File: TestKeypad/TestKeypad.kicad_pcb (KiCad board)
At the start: 2 copper layers, 78.7 x 92.7 mm, 71 parts, among them J1 Mini-DIN-6, Q1 2N7000, SW1 SW_SPST, SW10 SW_SPST, SW11 SW_SPST, SW12 SW_SPST, SW13 SW_SPST, SW14 SW_SPST, SW15 SW_SPST, SW16 SW_SPST, SW2 SW_SPST, SW3 SW_SPST, SW4 SW_SPST, SW5 SW_SPST, SW6 SW_SPST, SW7 SW_SPST, SW8 SW_SPST, SW9 SW_SPST, U1 ATtiny24A-PU

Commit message: Finalise test keypad r01 and silkscreen
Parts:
- added REF**: OSHW Logo, Symbol:OSHW-Symbol_6.7x6mm_SilkScreen, F.Cu at (177.5, 69.8)
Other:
- board text added: "JLCJLCJLCJLC"
- board text added: "Order:"
- board text added: "PS2KB Testpad"
- board text added: "r01"

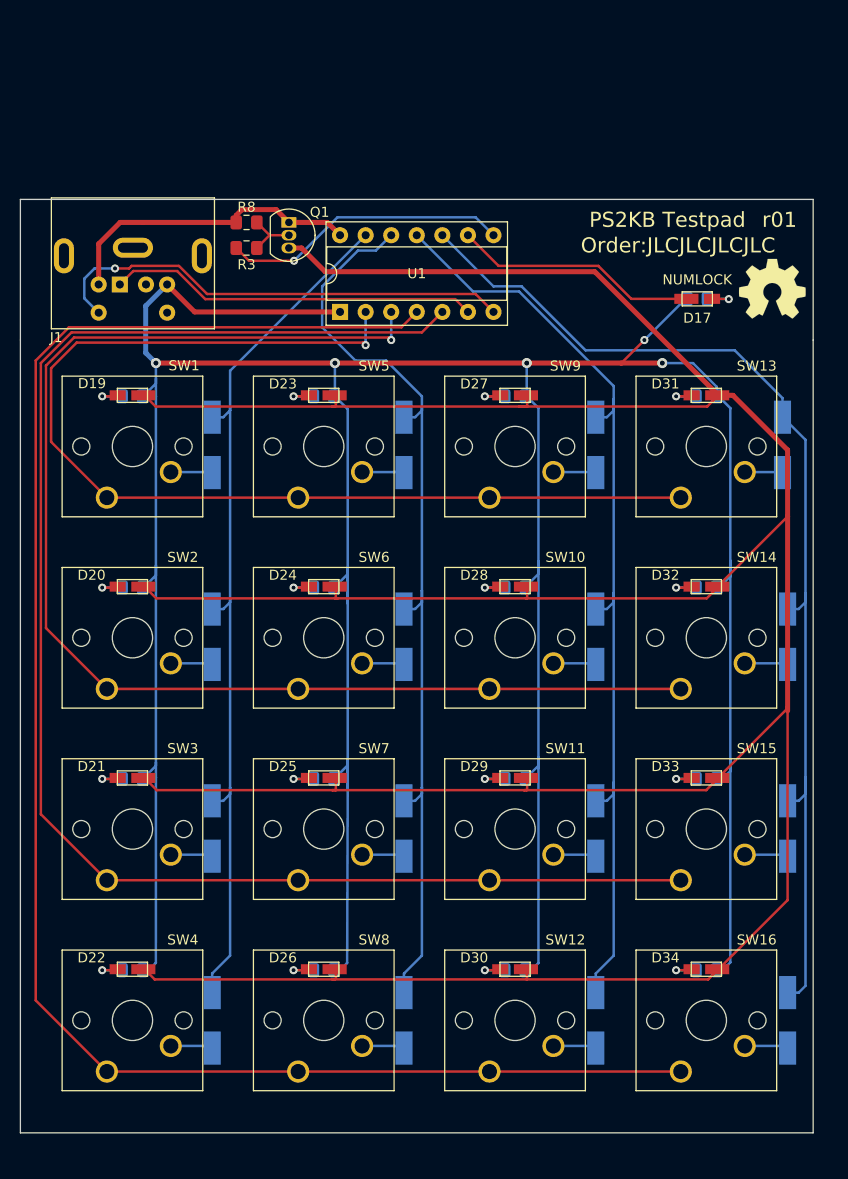
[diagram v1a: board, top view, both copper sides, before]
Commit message: Revise test keypad to r02
Updated components to match the actual board and revised PCB layout
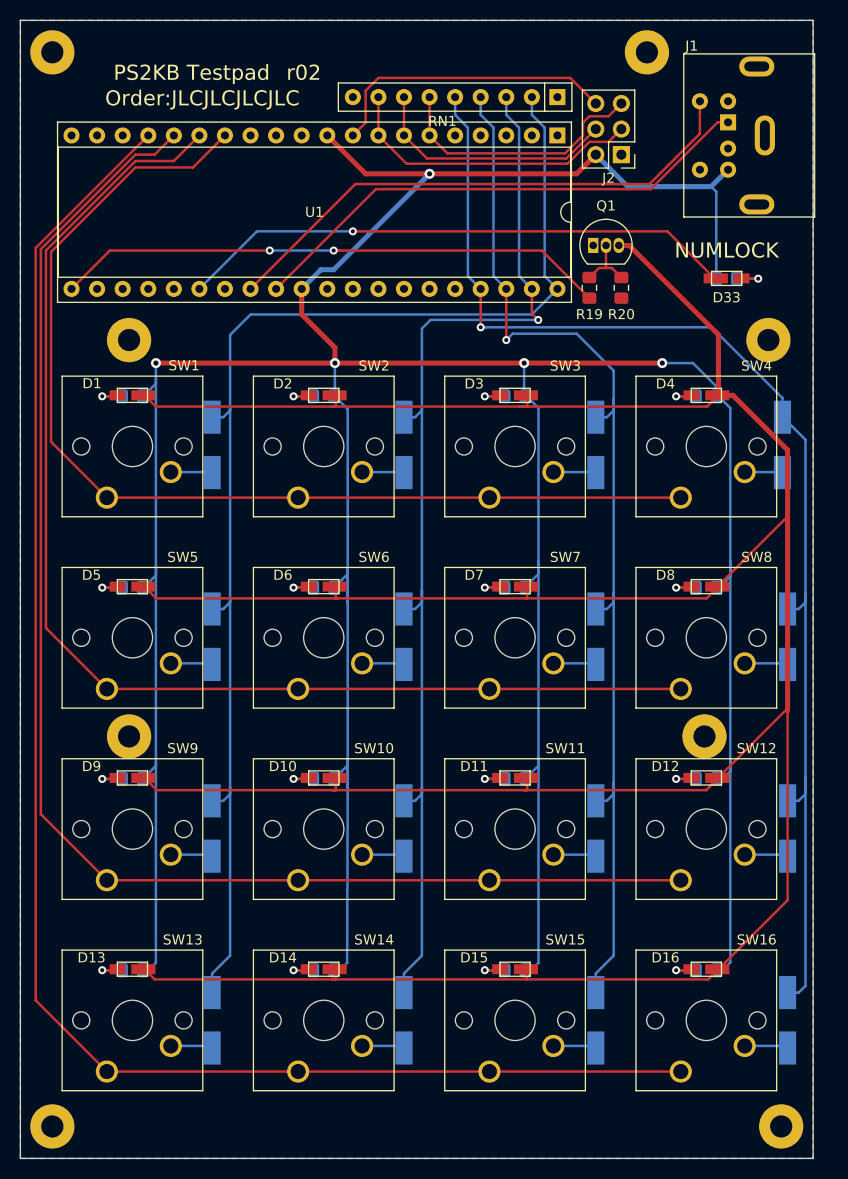
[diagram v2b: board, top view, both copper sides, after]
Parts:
- removed the REF** at (177.5, 69.8)
- added J2: ISP Header, Connector_PinHeader_2.54mm:PinHeader_2x03_P2.54mm_Vertical, F.Cu at (162.6, 56.5)
- added REF**: MountingHole_2.2mm_M2_Pad, MountingHole:MountingHole_2.2mm_M2_Pad, F.Cu at (113.7, 114.3)
- added REF**: MountingHole_2.2mm_M2_Pad, MountingHole:MountingHole_2.2mm_M2_Pad, F.Cu at (170.8, 114.3)
- added REF**: MountingHole_2.2mm_M2_Pad, MountingHole:MountingHole_2.2mm_M2_Pad, F.Cu at (106.0, 153.0)
- added REF**: MountingHole_2.2mm_M2_Pad, MountingHole:MountingHole_2.2mm_M2_Pad, F.Cu at (178.4, 153.0)
- added REF**: MountingHole_2.2mm_M2_Pad, MountingHole:MountingHole_2.2mm_M2_Pad, F.Cu at (177.2, 74.9)
- added REF**: MountingHole_2.2mm_M2_Pad, MountingHole:MountingHole_2.2mm_M2_Pad, F.Cu at (113.7, 74.9)
- added REF**: MountingHole_2.2mm_M2_Pad, MountingHole:MountingHole_2.2mm_M2_Pad, F.Cu at (165.1, 46.4)
- added REF**: MountingHole_2.2mm_M2_Pad, MountingHole:MountingHole_2.2mm_M2_Pad, F.Cu at (106.0, 46.4)
- added RN1: 100k, Resistor_THT:R_Array_SIP9, F.Cu at (156.2, 50.8)
- U1: value ATtiny24A-PU -> ATmega8535-16PU; footprint Package_DIP:DIP-14_W7.62mm_Socket -> Package_DIP:DIP-40_W15.24mm_Socket
- moved J1 62.5 mm to (175.3, 54.6), turned to 90 degrees
- moved R20 37.8 mm to (162.6, 69.7), turned to 270 degrees
- moved R19 34.3 mm to (159.4, 69.7), turned to 90 degrees
- moved Q1 30.3 mm to (159.8, 65.5), turned to 0 degrees
- moved U1 27.8 mm to (156.2, 54.6), turned to 270 degrees
- moved D33 3.56 mm to (173.0, 68.8)
- moved R17 3.56 mm to (173.0, 68.8)
- renumbered D19 to D1, D25 to D10, D29 to D11, D33 to D12, D22 to D13, D26 to D14, D30 to D15, D34 to D16, D1 to D17, D5 to D18, D9 to D19, D23 to D2, D13 to D20, D2 to D21, D6 to D22, D10 to D23, D14 to D24, D3 to D25, D7 to D26, D11 to D27, D15 to D28, D4 to D29, D27 to D3, D8 to D30, D12 to D31, D16 to D32, D17 to D33, D31 to D4, D20 to D5, D24 to D6, D28 to D7, D32 to D8, D21 to D9, R4 to R1, R11 to R10, R15 to R11, R19 to R12, R7 to R13, R12 to R14, R16 to R15, R20 to R16, R1 to R17, R3 to R19, R9 to R2, R8 to R20, R13 to R3, R17 to R4, R10 to R6, R14 to R7, R18 to R8, R6 to R9, SW7 to SW10, SW15 to SW12, SW4 to SW13, SW8 to SW14, SW12 to SW15, SW5 to SW2, SW9 to SW3, SW13 to SW4, SW2 to SW5, SW10 to SW7, SW14 to SW8, SW3 to SW9
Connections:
- D33 pad 1: Net-(D17-Pad1) -> Net-(D33-Pad1)
- J1 pad 3: Earth -> GND
- R19 pad 1: Net-(Q1-Pad2) -> /Counter2A-PWM
- R19 pad 2: /LED-PWM -> Net-(Q1-Pad2)
- U1 pad 1: 5v -> Earth
- U1 pad 10: D -> 5v
- U1 pad 11: C -> Earth
- U1 pad 12: B -> Net-(U1-Pad12)
- U1 pad 13: A -> Net-(U1-Pad13)
- U1 pad 14: Earth -> 1
- U1 pad 2: 1 -> Earth
- U1 pad 3: 2 -> Earth
- U1 pad 4: 4 -> Earth
- U1 pad 5: 3 -> Earth
- U1 pad 6: /Data -> Net-(J2-Pad5)
- U1 pad 7: /Clk -> Net-(J2-Pad4)
- U1 pad 8: /LED-PWM -> Net-(J2-Pad3)
- U1 pad 9: Net-(D17-Pad1) -> Net-(J2-Pad6)
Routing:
- net Net-(D33-Pad1): track 0.00 -> 55.5 mm, vias 0 -> 1
- net /Counter2A-PWM: track 0.00 -> 55.0 mm, vias 0 -> 2
- net 5v: track 368.6 -> 411.8 mm
- net A: track 89.1 -> 128.1 mm
- net Earth: track 30.9 -> 0.00 mm
- net Net-(J2-Pad3): track 0.00 -> 30.5 mm
- net Net-(J2-Pad6): track 0.00 -> 29.4 mm
- net Net-(D1-Pad1): track 375.0 -> 345.9 mm
- net /LED-PWM: track 28.8 -> 0.00 mm, vias 1 -> 0
- net Net-(J2-Pad5): track 0.00 -> 26.4 mm
- net Net-(J2-Pad4): track 0.00 -> 25.0 mm
- net Net-(D17-Pad1): track 24.2 -> 0.00 mm
- net B: track 94.1 -> 110.4 mm, vias 0 -> 1
- net D: track 108.5 -> 124.9 mm, vias 0 -> 1
- net /Data: track 36.8 -> 51.7 mm
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- added copper zone on B.Cu, net Earth
- added copper zone on F.Cu, net Earth
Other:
- board size 78.7 x 92.7 mm -> 78.7 x 113 mm
- board text added: "r02"
- board text removed: "r01"

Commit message: Revise test keypad to r03
Tweaked just before making a production run
Added screw holes
Added an ISP header
Added pulldown resistor array to switch input lines
Also remapped an incorrectly-placed "GND" label to the actual ground net (which slipped through into the production run)
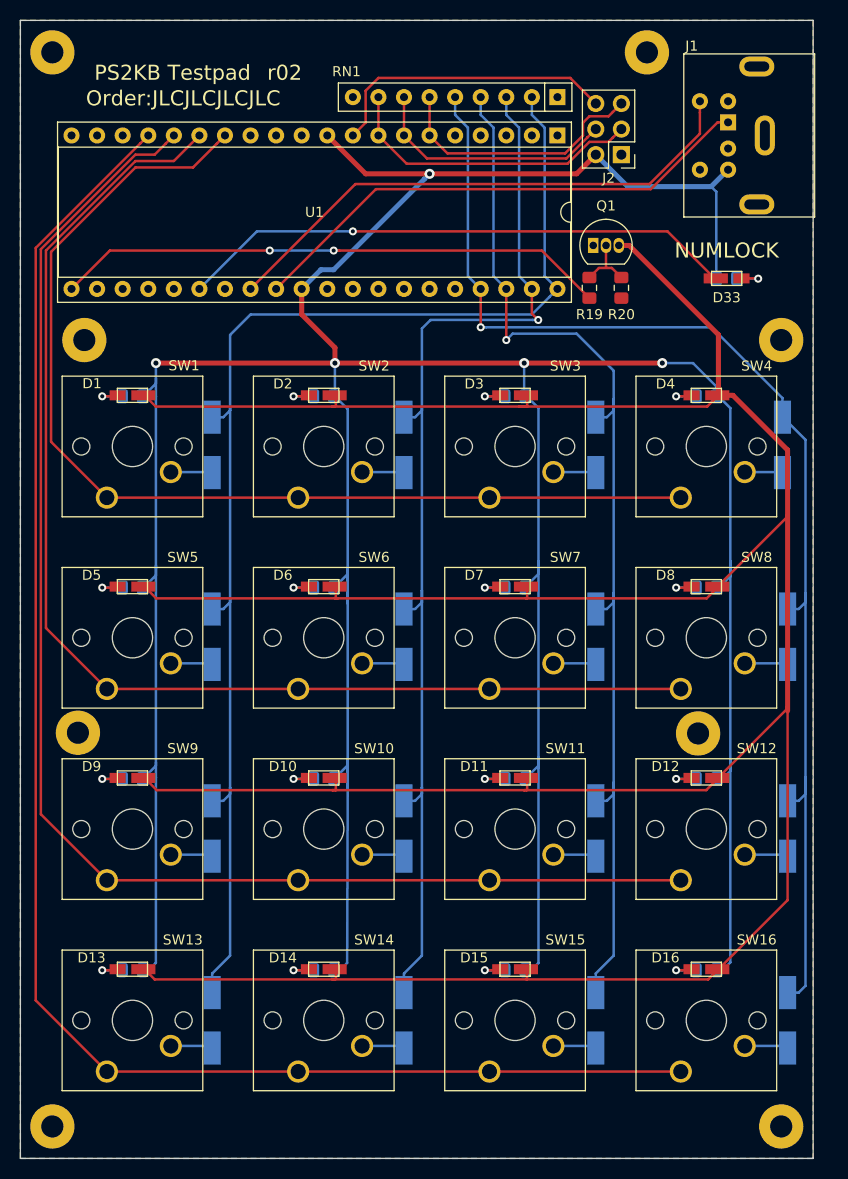
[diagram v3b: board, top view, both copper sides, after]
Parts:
- moved REF** 5.09 mm to (108.6, 113.9)
- moved REF** 4.45 mm to (109.2, 74.9)
- moved REF** 1.27 mm to (178.4, 74.9)
- moved REF** 0.70 mm to (170.2, 114.0)
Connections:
- J1 pad 3: GND -> Earth

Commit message: Update keypad also
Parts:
- removed RN1: 100k, Resistor_THT:R_Array_SIP9
- D17, D18, D19, D20, D21, D22, D23, D24, D25, D26, D27, D28, D29, D30, D31, D32: footprint Diode_SMD:D_MiniMELF_Handsoldering -> Diode_SMD:D_MiniMELF
- turned D17 to 90 degrees
- turned D18 to 90 degrees
- turned D19 to 90 degrees
- turned D20 to 90 degrees
- turned D21 to 90 degrees
- turned D22 to 90 degrees
- turned D23 to 90 degrees
- turned D24 to 90 degrees
- turned D25 to 90 degrees
- turned D26 to 90 degrees
- turned D27 to 90 degrees
- turned D28 to 90 degrees
- turned D29 to 90 degrees
- turned D30 to 90 degrees
- turned D31 to 90 degrees
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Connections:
- D17 pad 1: A -> Net-(D17-Pad1)
- D17 pad 2: Net-(D17-Pad2) -> A
- D18 pad 1: B -> Net-(D18-Pad1)
- D18 pad 2: Net-(D18-Pad2) -> B
- D19 pad 1: C -> Net-(D19-Pad1)
- D19 pad 2: Net-(D19-Pad2) -> C
- D20 pad 1: D -> Net-(D20-Pad1)
- D20 pad 2: Net-(D20-Pad2) -> D
- D21 pad 1: A -> Net-(D21-Pad1)
- D21 pad 2: Net-(D21-Pad2) -> A
- D22 pad 1: B -> Net-(D22-Pad1)
- D22 pad 2: Net-(D22-Pad2) -> B
- D23 pad 1: C -> Net-(D23-Pad1)
- D23 pad 2: Net-(D23-Pad2) -> C
- D24 pad 1: D -> Net-(D24-Pad1)
- D24 pad 2: Net-(D24-Pad2) -> D
- D25 pad 1: A -> Net-(D25-Pad1)
- D25 pad 2: Net-(D25-Pad2) -> A
- D26 pad 1: B -> Net-(D26-Pad1)
- D26 pad 2: Net-(D26-Pad2) -> B
- D27 pad 1: C -> Net-(D27-Pad1)
- D27 pad 2: Net-(D27-Pad2) -> C
- D28 pad 1: D -> Net-(D28-Pad1)
- D28 pad 2: Net-(D28-Pad2) -> D
- D29 pad 1: A -> Net-(D29-Pad1)
- D29 pad 2: Net-(D29-Pad2) -> A
- D30 pad 1: B -> Net-(D30-Pad1)
- D30 pad 2: Net-(D30-Pad2) -> B
- D31 pad 1: C -> Net-(D31-Pad1)
- D31 pad 2: Net-(D31-Pad2) -> C
- D32 pad 1: D -> Net-(D32-Pad1)
- D32 pad 2: Net-(D32-Pad2) -> D
- SW1 pad 2: Net-(D17-Pad2) -> Net-(D17-Pad1)
- SW10 pad 2: Net-(D26-Pad2) -> Net-(D26-Pad1)
- SW11 pad 2: Net-(D27-Pad2) -> Net-(D27-Pad1)
- SW12 pad 2: Net-(D28-Pad2) -> Net-(D28-Pad1)
- SW13 pad 2: Net-(D29-Pad2) -> Net-(D29-Pad1)
- SW14 pad 2: Net-(D30-Pad2) -> Net-(D30-Pad1)
- SW15 pad 2: Net-(D31-Pad2) -> Net-(D31-Pad1)
- SW16 pad 2: Net-(D32-Pad2) -> Net-(D32-Pad1)
- SW2 pad 2: Net-(D18-Pad2) -> Net-(D18-Pad1)
- SW3 pad 2: Net-(D19-Pad2) -> Net-(D19-Pad1)
- SW4 pad 2: Net-(D20-Pad2) -> Net-(D20-Pad1)
- SW5 pad 2: Net-(D21-Pad2) -> Net-(D21-Pad1)
- SW6 pad 2: Net-(D22-Pad2) -> Net-(D22-Pad1)
- SW7 pad 2: Net-(D23-Pad2) -> Net-(D23-Pad1)
- SW8 pad 2: Net-(D24-Pad2) -> Net-(D24-Pad1)
- SW9 pad 2: Net-(D25-Pad2) -> Net-(D25-Pad1)
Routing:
- net C: track 109.5 -> 89.6 mm
- net D: track 124.9 -> 105.3 mm
- net A: track 128.1 -> 117.4 mm
- net B: track 110.4 -> 100.6 mm
- net Net-(D24-Pad1): track 0.00 -> 4.63 mm
- net Net-(D28-Pad1): track 0.00 -> 4.61 mm
- net Net-(D19-Pad1): track 0.00 -> 4.60 mm
- net Net-(D32-Pad1): track 0.00 -> 4.59 mm
- net Net-(D23-Pad1): track 0.00 -> 4.58 mm
- net Net-(D27-Pad1): track 0.00 -> 4.56 mm
- net Net-(D18-Pad1): track 0.00 -> 4.55 mm
- net Net-(D31-Pad1): track 0.00 -> 4.54 mm
- net Net-(D22-Pad1): track 0.00 -> 4.53 mm
- net Net-(D26-Pad1): track 0.00 -> 4.51 mm
- net Net-(D17-Pad1): track 0.00 -> 4.50 mm
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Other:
- board text added: "r03"
- board text removed: "r02"

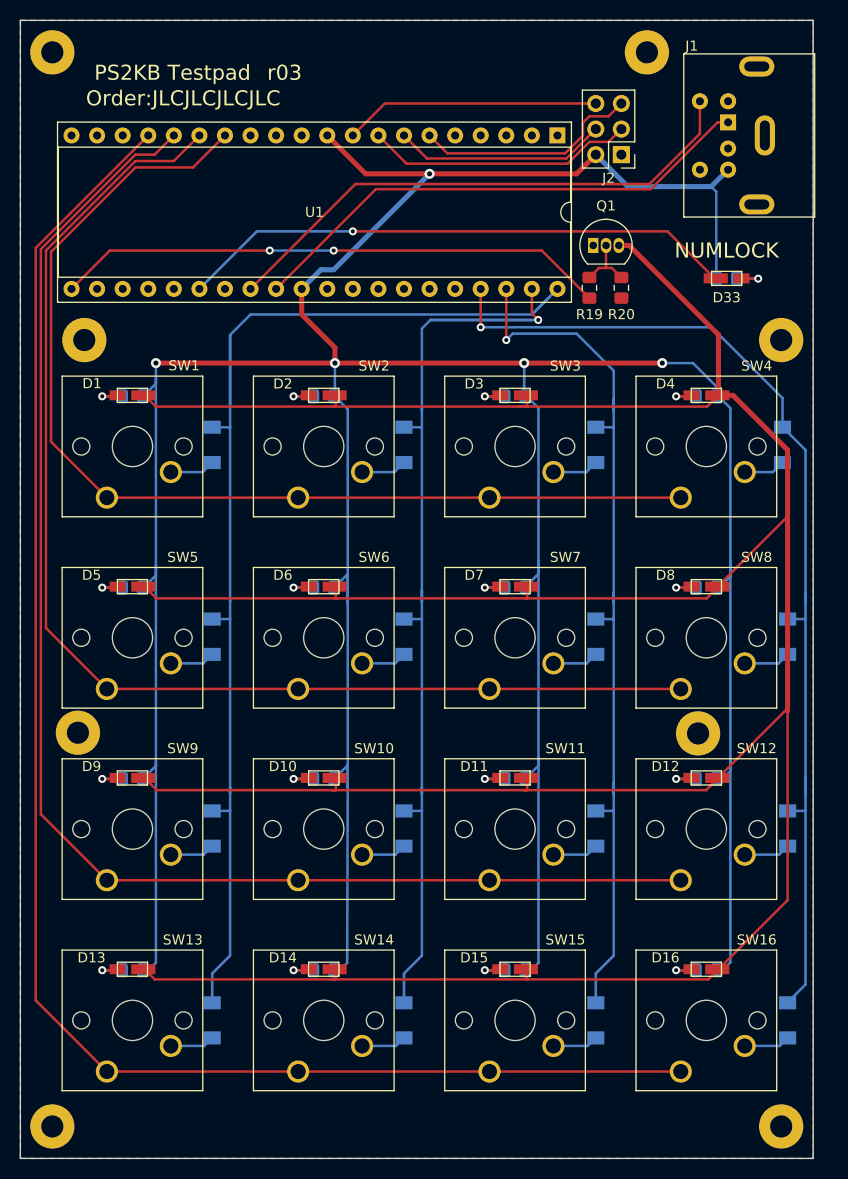
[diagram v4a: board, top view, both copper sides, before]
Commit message: Revise test keypad to r04
Flipped numlock LED to the back of the board, using it as a diffuser
Added design to blank area at the top
Rounded off the corners
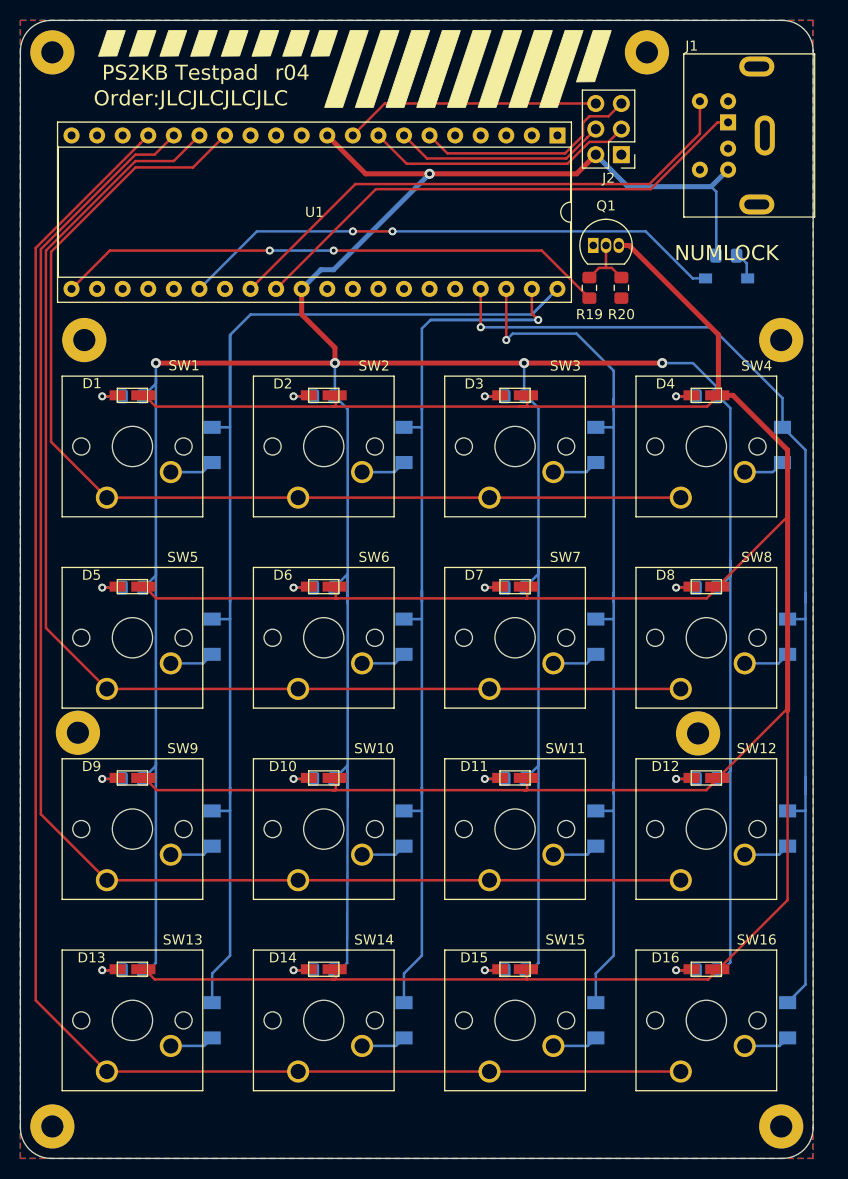
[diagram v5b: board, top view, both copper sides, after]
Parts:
- D33: moved to B.Cu
- moved R17 2.26 mm to (173.0, 66.5)
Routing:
- net 5v: track 409.4 -> 407.1 mm
- net Net-(D33-Pad2): track 3.80 -> 2.85 mm, vias 1 -> 0
- net Net-(D33-Pad1): track 55.5 -> 54.8 mm, vias 1 -> 2
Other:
- outline, holes or cut-outs redrawn
- board text added: "r04"
- board text removed: "r03"
